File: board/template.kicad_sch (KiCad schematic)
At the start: 0 parts

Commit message: Basic circuit that is provided by drew
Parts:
- added C2: 10uF, Capacitor_SMD:CP_Elec_5x5.8, symbol Device:C_Polarized_US
- added C4: 1uF, Capacitor_SMD:C_0603_1608Metric, symbol Device:C
- added C7: 1.5nF, Capacitor_SMD:C_0603_1608Metric, symbol Device:C
- added C8: 0.1uF, Capacitor_SMD:C_0603_1608Metric, symbol Device:C
- added D2: D_Photo_Filled, symbol Device:D_Photo_Filled
- added R2: 1.5k, Resistor_SMD:R_0603_1608Metric, symbol Device:R_US
- added R3: 100k, Resistor_SMD:R_0603_1608Metric, symbol Device:R_US
- added R6, R9: 10k, Resistor_SMD:R_0603_1608Metric, symbol Device:R_US
- added TP1: V_{P_PD}=I_{PD}*R_{f}+V_{bias}, TestPoint:TestPoint_Pad_D1.5mm, symbol Connector:TestPoint
- added TP2: 2.5V_{ref}, TestPoint:TestPoint_Pad_D1.5mm, symbol Connector:TestPoint
- added U2: OPA4192, Package_SO:SOIC-14_3.9x8.7mm_P1.27mm, symbol Device:Opamp_Quad
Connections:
- new net: C2.1, R3.2, U2.10 (+)
- new net: C4.1, R6.1, U2.9 (-)
- new net: C7.2, D2.1 (K), R9.2, U2.13 (-)
- new net: R2.2, R3.1, U2.6 (K), U2.8 (K)
- new net +10V: R2.1
- new net GND: C2.2, C8.2, D2.2 (A), U2.4 (A)
- new net V_{P_PD}: C7.1, R9.1, TP1.1, U2.14
- new net v_{ref}: C4.2, C8.1, R6.2, TP2.1, U2.12 (+), U2.8
- no-connect marks 0 -> 1

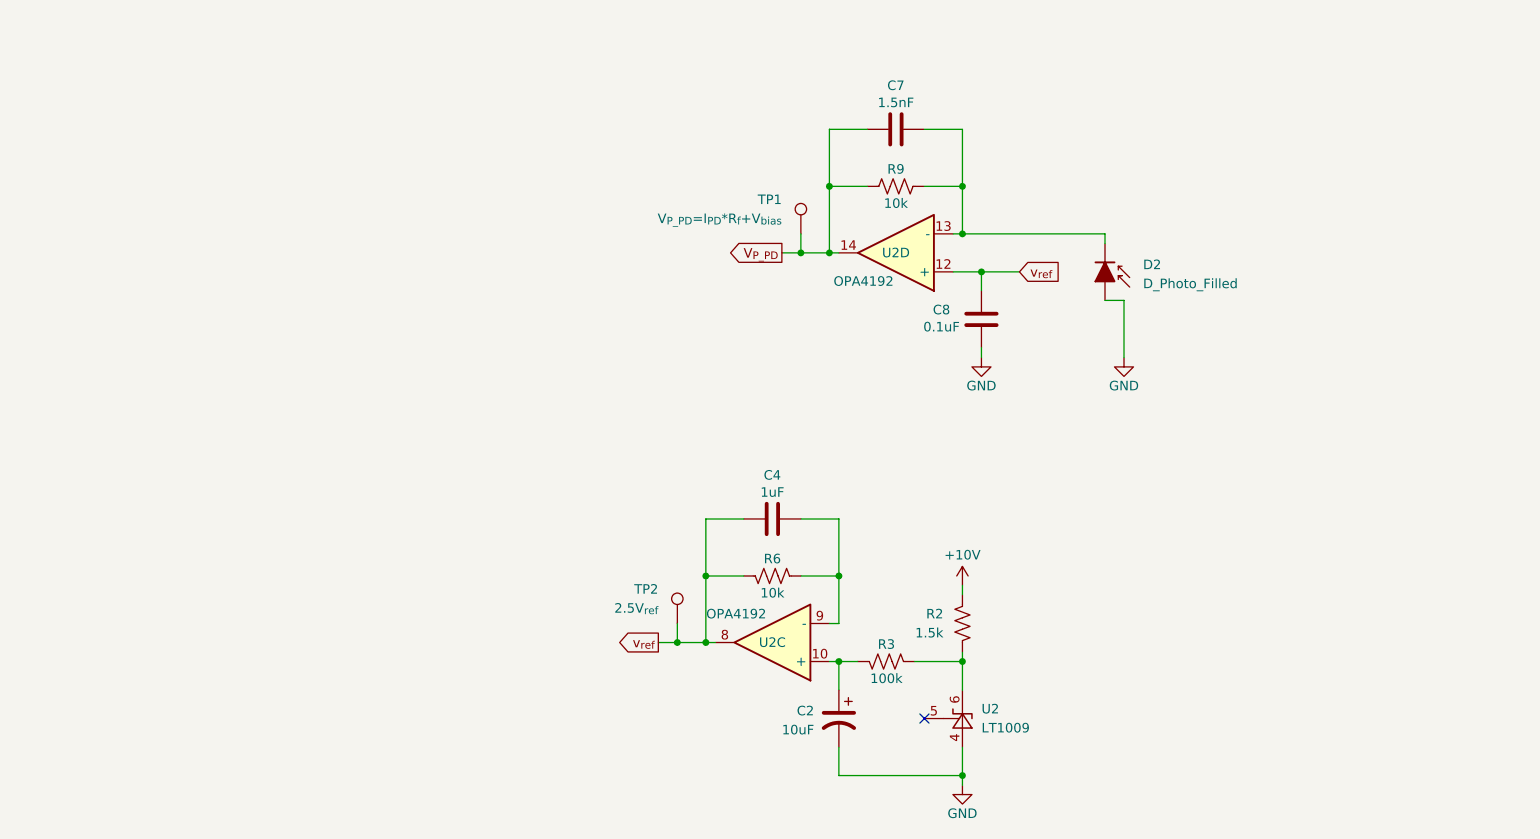
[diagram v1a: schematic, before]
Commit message: added teensy found the OPAMP
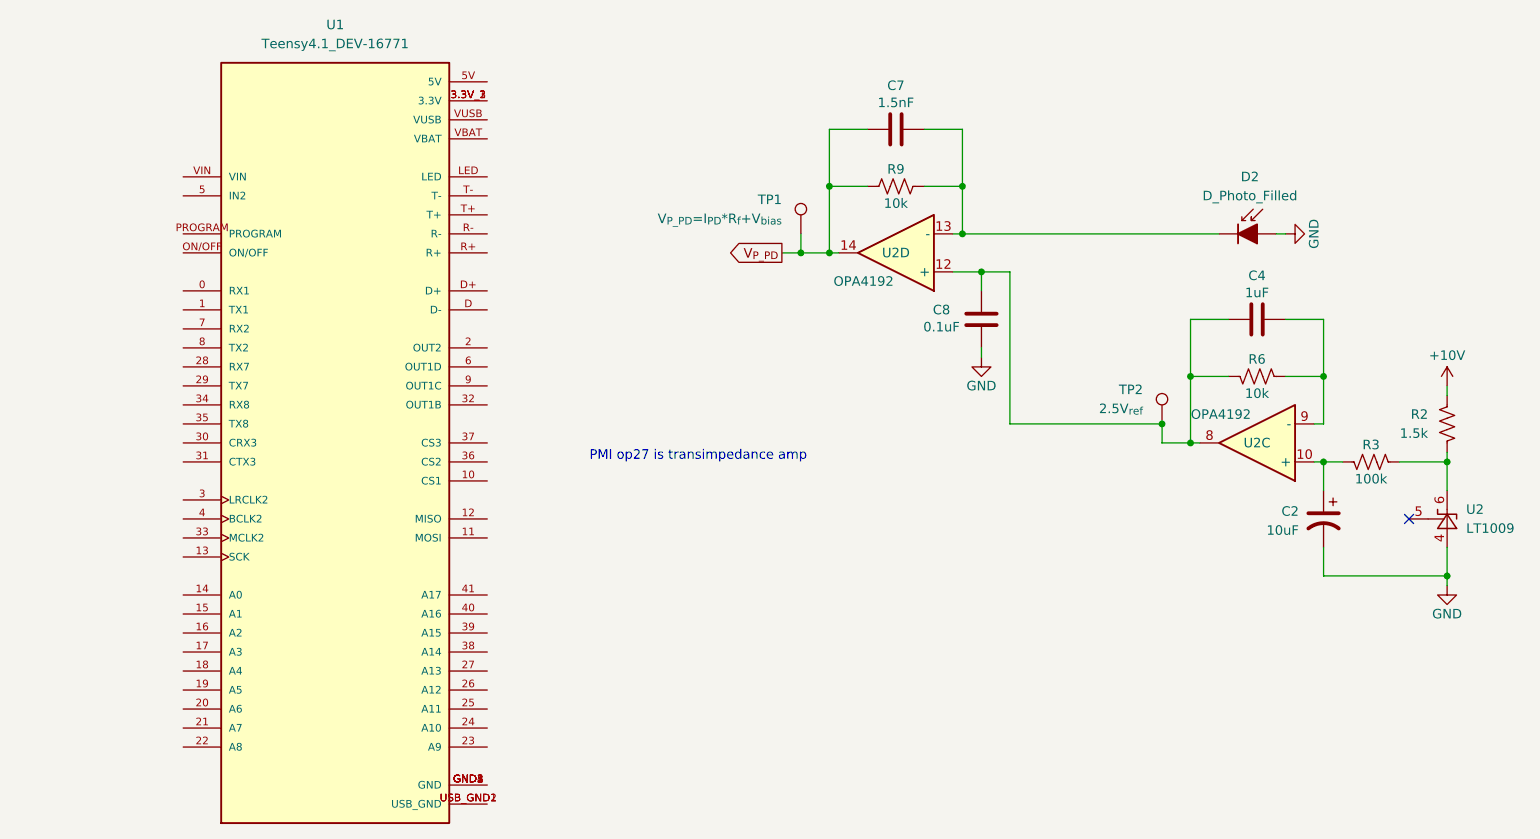
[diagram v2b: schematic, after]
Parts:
- added U1: Teensy4.1_DEV-16771, MRDT_Shields:Teensy_4_1_Ethernet, symbol MRDT_Shields:Teensy4.1_DEV-16771
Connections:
- net v_{ref}: no longer names the net of C4.2, C8.1, R6.2, TP2.1, U2.12 (+), U2.8
- new net: U1.3.3V_1 (3.3V), U1.3.3V_2 (3.3V), U1.3.3V_3 (3.3V)
- new net: U1.GND1 (GND), U1.GND2 (GND), U1.GND3 (GND), U1.GND4 (GND), U1.GND5 (GND)
- new net: U1.USB_GND1 (USB_GND), U1.USB_GND2 (USB_GND)
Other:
- note added: "PMI op27 is transimpedance amp"
- moved on the sheet: C2, C4, D2, R2, R3, R6, TP2, U2, U2C

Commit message: figured out teensy pin to be used
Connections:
- net UART: now reaches U1.1 (TX1)
- net at U1.24 (A10): now also U1.25 (A11)
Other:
- note added: "Using pin1 on other board for UART"
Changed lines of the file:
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@@
 	(generator_version "9.0")
 	(paper "A4")
+	(text "Using pin1 on other board for UART"
+		(exclude_from_sim no)
+		(at 95.25 81.788 0)
+		(effects
+			(font
+				(size 1.27 1.27)
+			)
+		)
+	)
 	(text "PMI op27 is transimpedance amp"
 		(exclude_from_sim no)
@@
 	(wire
 		(pts
+			(xy 77.47 137.16) (xy 77.47 139.7)
+		)
+		(stroke
+			(width 0)
+			(type default)
+		)
+	)
+	(wire
+		(pts
 			(xy 205.74 102.87) (xy 205.74 104.14)
 		)
@@
 	(wire
 		(pts
+			(xy 36.83 83.82) (xy 22.86 83.82)
+		)
+		(stroke
+			(width 0)
+			(type default)
+		)
+	)
+	(wire
+		(pts
 			(xy 171.45 101.6) (xy 167.64 101.6)
 		)
@@
 	(wire
 		(pts
+			(xy 22.86 83.82) (xy 22.86 82.55)
+		)
+		(stroke
+			(width 0)
+			(type default)
+		)
+	)
+	(wire
+		(pts
 			(xy 187.96 99.06) (xy 189.23 99.06)
 		)
@@
 		)
 	)
+	(global_label "UART"
+		(shape input)
+		(at 22.86 82.55 180)
+		(fields_autoplaced yes)
+		(effects
+			(font
+				(size 1.27 1.27)
+			)
+			(justify right)
+		)
+		(property "Intersheetrefs" "${INTERSHEET_REFS}"
+			(at 15.2181 82.55 0)
+			(effects
+				(font
+					(size 1.27 1.27)
+				)
+				(justify right)
+				(hide yes)
+			)
+		)
+	)
